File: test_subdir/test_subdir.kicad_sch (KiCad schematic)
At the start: 12 parts, among them J1 Conn_01x08_Male, J2 Conn_01x08_Male, J3 Conn_01x08_Male, J4 USB_B, J5 Conn_01x08_Male, J6 Conn_01x06_Male, U1 FT2232H, Y1 12 MHz

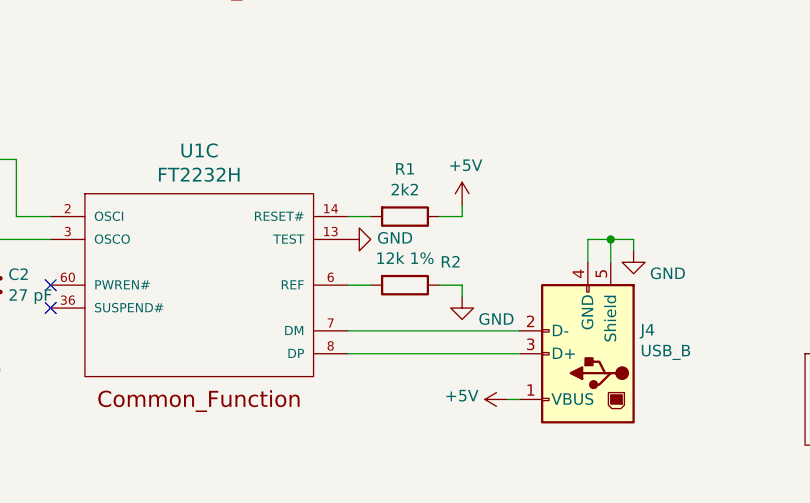
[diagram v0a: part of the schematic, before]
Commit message: [Fixed] Use of "12k 1%" which is currently discouraged
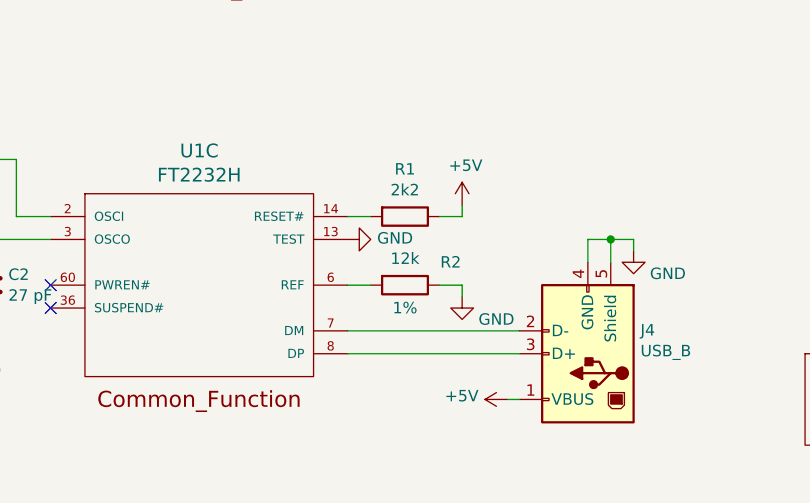
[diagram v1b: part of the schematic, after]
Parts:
- R2: value 12k 1% -> 12k; Tolerance (none) -> 1%
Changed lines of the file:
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@@
 			)
 		)
-		(property "Value" "12k 1%"
+		(property "Value" "12k"
 			(at 111.76 120.2436 90)
 			(effects
@@
 			)
 		)
+		(property "Tolerance" "1%"
+			(at 111.76 125.73 90)
+			(effects
+				(font
+					(size 1.27 1.27)
+				)
+			)
+		)

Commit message: Set R1 tolerance to 5%
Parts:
- R1: Tolerance (none) -> 5%
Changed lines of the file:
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@@
+			)
+		)
+		(property "Tolerance" "5%"
+			(at 111.76 115.57 90)
+			(effects
+				(font
+					(size 1.27 1.27)
+				)
+				(hide yes)
 			)
 		)
